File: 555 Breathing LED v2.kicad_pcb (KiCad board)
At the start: 2 copper layers, 80.8 x 35.6 mm, 17 parts, among them Q1 PN2222A, SW1 SW_SPDT, U1 LMC555xN

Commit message: Updated, epic fortnite
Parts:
- added D2: 1N4148, Diode_THT:D_DO-35_SOD27_P7.62mm_Horizontal, F.Cu at (76.2, 73.7)
- added REF**: Switch Indicator, Local:Switch Indicator, F.Cu at (53.3, 81.3)
- added REF**: Standoff_M2x0.4, Local:Standoff_M2x0.4, F.Cu at (82.7, 95.1)
- BT1: footprint 555-Breathing-LED-v2:BatteryHolder_MPD_BA9VPC_1xPP3noholes -> Local:BatteryHolder_MPD_BA9VPC_1xPP3noholes
- R2: value 220 -> 100
- moved C3 21.3 mm to (100.3, 82.5), turned to 270 degrees
- moved Q1 7.62 mm to (118.1, 88.9), turned to 225 degrees
- moved R2 7.62 mm to (66.0, 91.4)
- moved R3 7.62 mm to (66.0, 85.1)
- moved R4 7.62 mm to (66.0, 78.7)
- moved C2 6.98 mm to (107.3, 82.5)
- moved C1 4.62 mm to (114.9, 83.8), turned to 0 degrees
- moved ? 3.81 mm to (64.8, 96.8)
- moved ? 3.81 mm to (55.9, 95.2)
- moved REF** 3.81 mm to (61.0, 69.8)
- moved U1 2.84 mm to (87.6, 90.2)
- moved R1 0.64 mm to (98.4, 90.2)
- turned SW1 to 90 degrees
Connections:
- SW1 pad 1: Net-(BT1-Pad1) -> Net-(D2-Pad2)
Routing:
- net Net-(BT1-Pad1): track 81.1 -> 50.5 mm
- net VCC: track 91.5 -> 72.1 mm
- net Net-(C3-Pad1): track 15.5 -> 5.08 mm
- net Net-(D2-Pad2): track 0.00 -> 9.12 mm
- net Net-(C1-Pad1): track 18.2 -> 14.3 mm
- net Net-(D1-Pad1): track 77.3 -> 74.7 mm
- net Net-(C2-Pad1): track 35.5 -> 37.8 mm
- net Net-(R4-Pad2): track 6.88 -> 8.98 mm
- net Net-(R3-Pad2): track 28.6 -> 29.8 mm
- net out: track 8.67 -> 7.59 mm
- net Net-(D1-Pad2): track 9.94 -> 11.0 mm
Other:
- board size 80.8 x 35.6 mm -> 84.6 x 35.6 mm

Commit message: Updated export
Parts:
- moved REF** 1.27 mm to (54.6, 81.3)

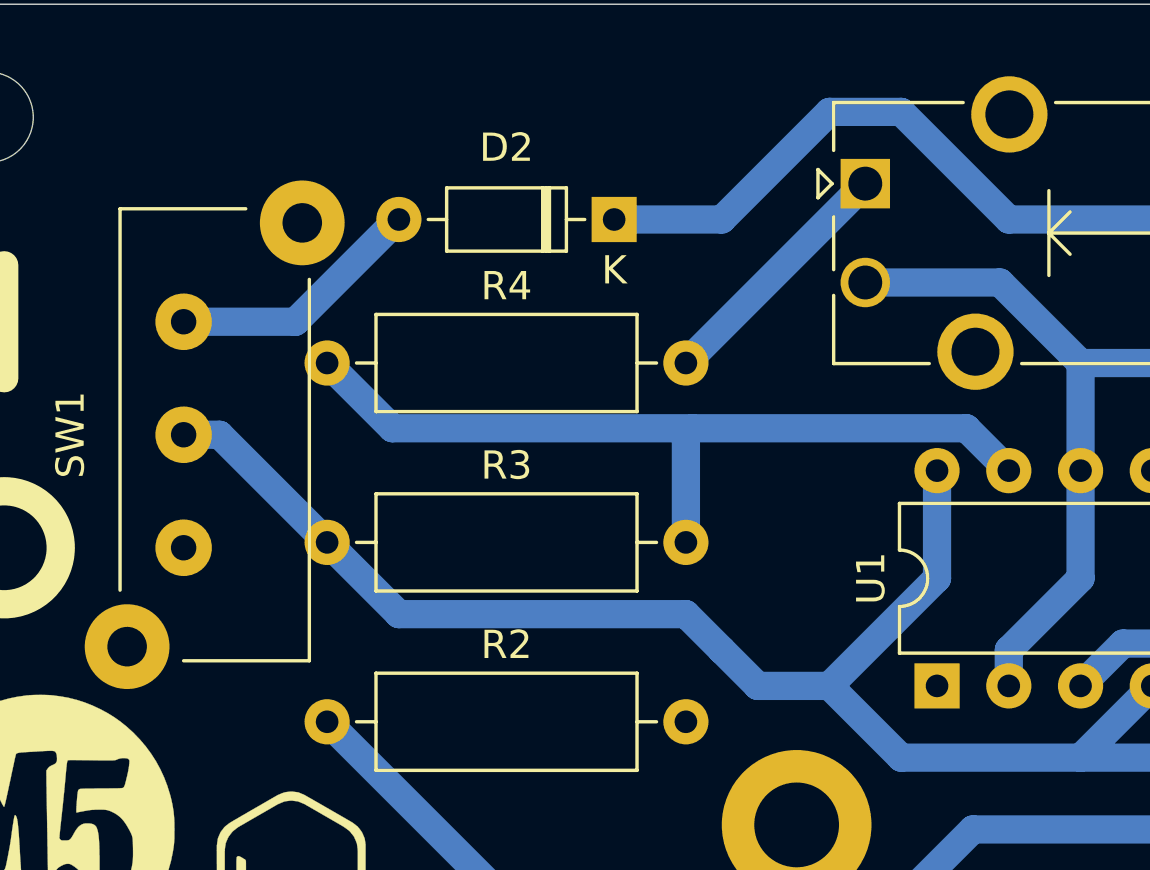
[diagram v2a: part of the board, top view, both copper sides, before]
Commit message: Fixed resistor placement error
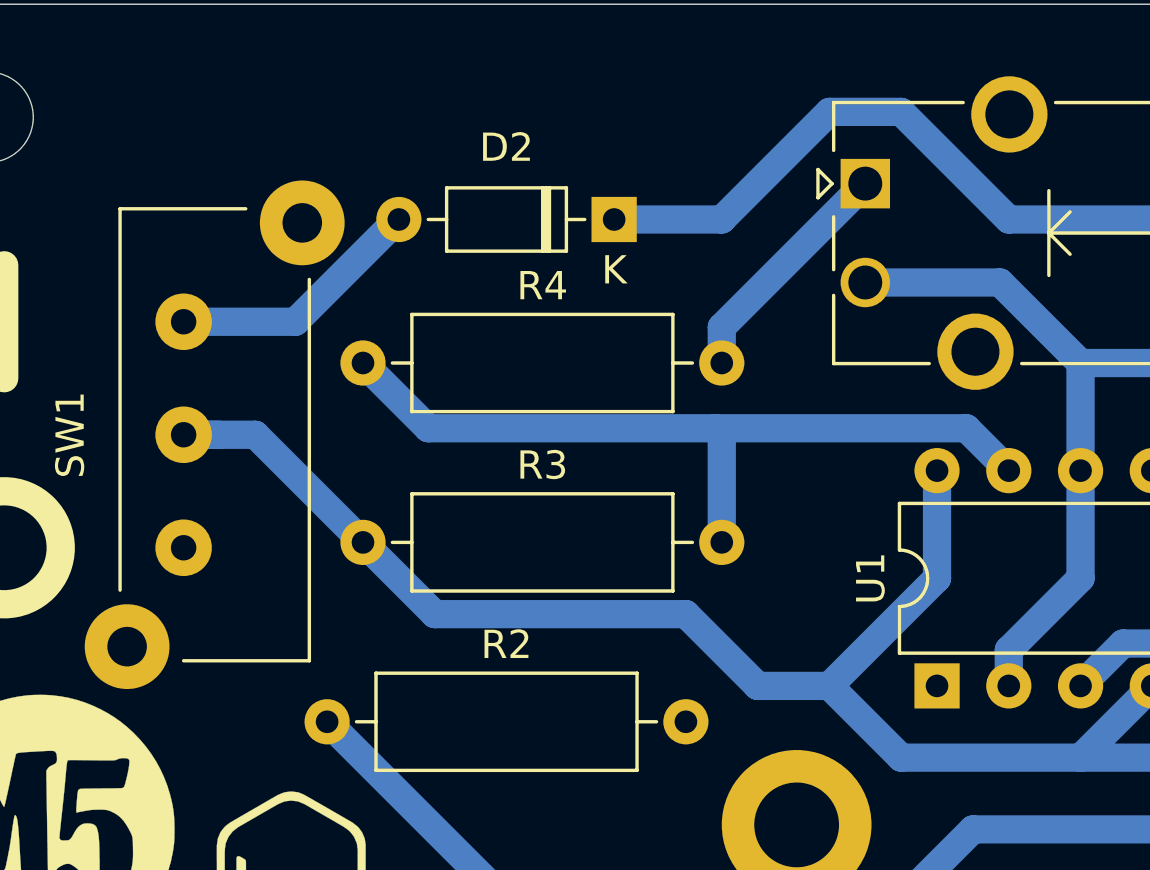
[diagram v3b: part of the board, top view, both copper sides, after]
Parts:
- moved R3 1.27 mm to (67.3, 85.1)
- moved R4 1.27 mm to (67.3, 78.7)
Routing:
- net Net-(R3-Pad2): track 29.8 -> 28.6 mm
- net VCC: track 72.1 -> 73.4 mm
- net Net-(R4-Pad2): track 8.98 -> 8.45 mm

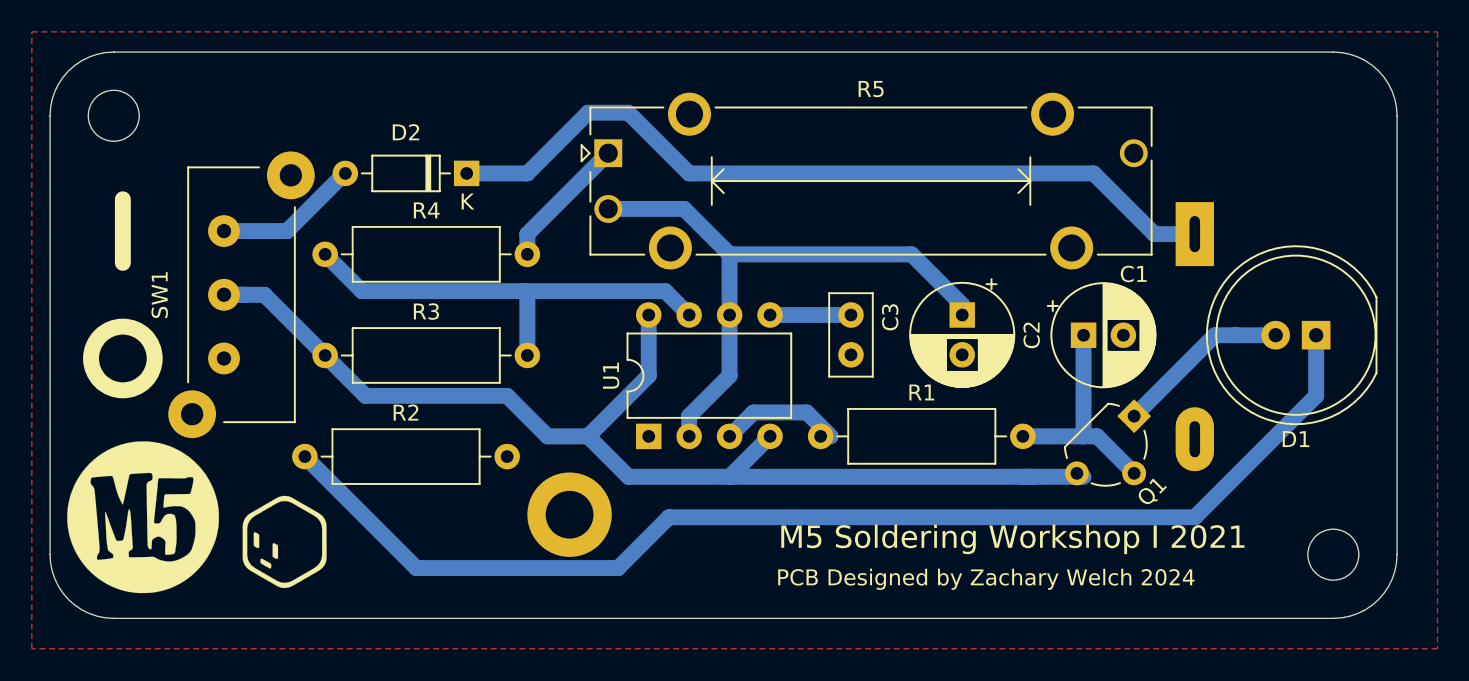
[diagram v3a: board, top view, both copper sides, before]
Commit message: fixed diode
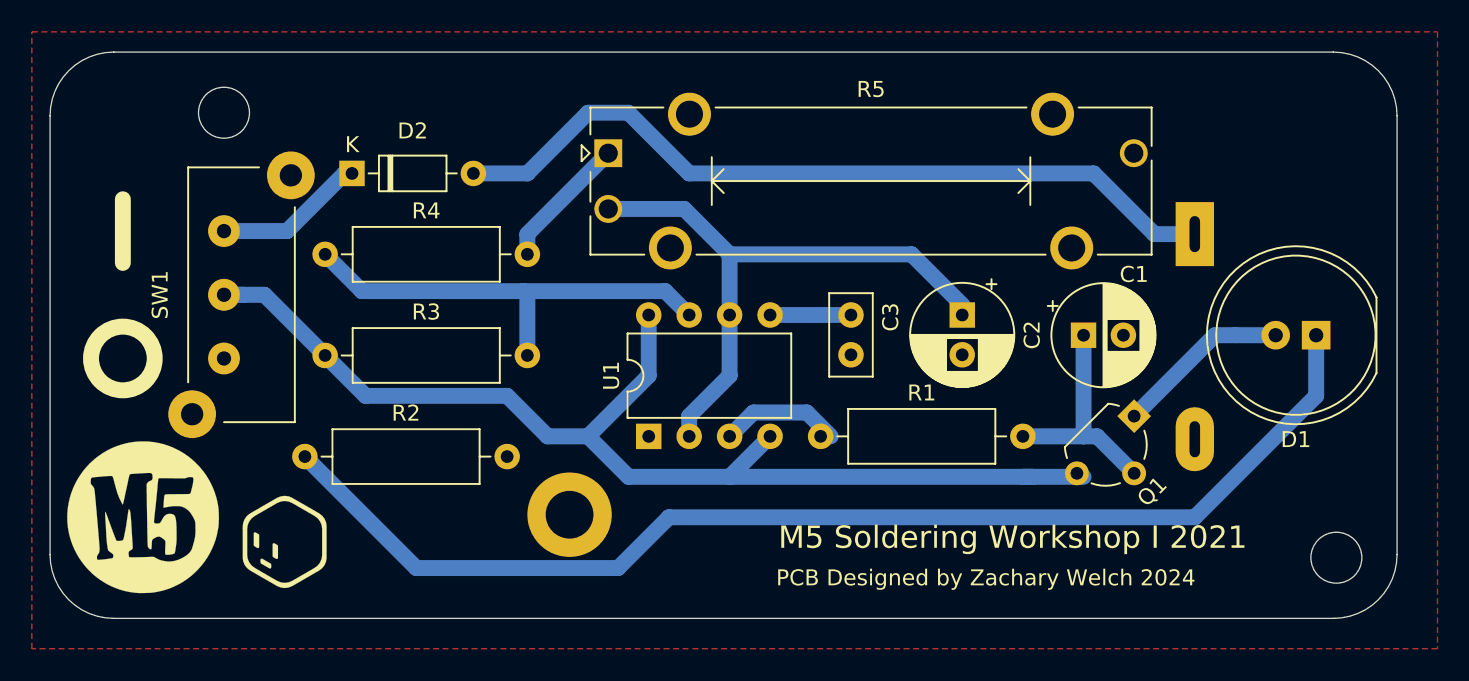
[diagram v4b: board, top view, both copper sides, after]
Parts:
- moved D2 7.20 mm to (69.0, 73.7), turned to 0 degrees
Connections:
- D2 pad 1: Net-(BT1-Pad1) -> Net-(D2-Pad1)
- D2 pad 2: Net-(D2-Pad2) -> Net-(BT1-Pad1)
- SW1 pad 1: Net-(D2-Pad2) -> Net-(D2-Pad1)
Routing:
- net Net-(D2-Pad2): track 9.12 -> 0.00 mm
- net Net-(D2-Pad1): track 0.00 -> 9.12 mm
